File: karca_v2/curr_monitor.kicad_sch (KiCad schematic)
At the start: 25 parts, among them U30 INA180A4, U32 NUP4202

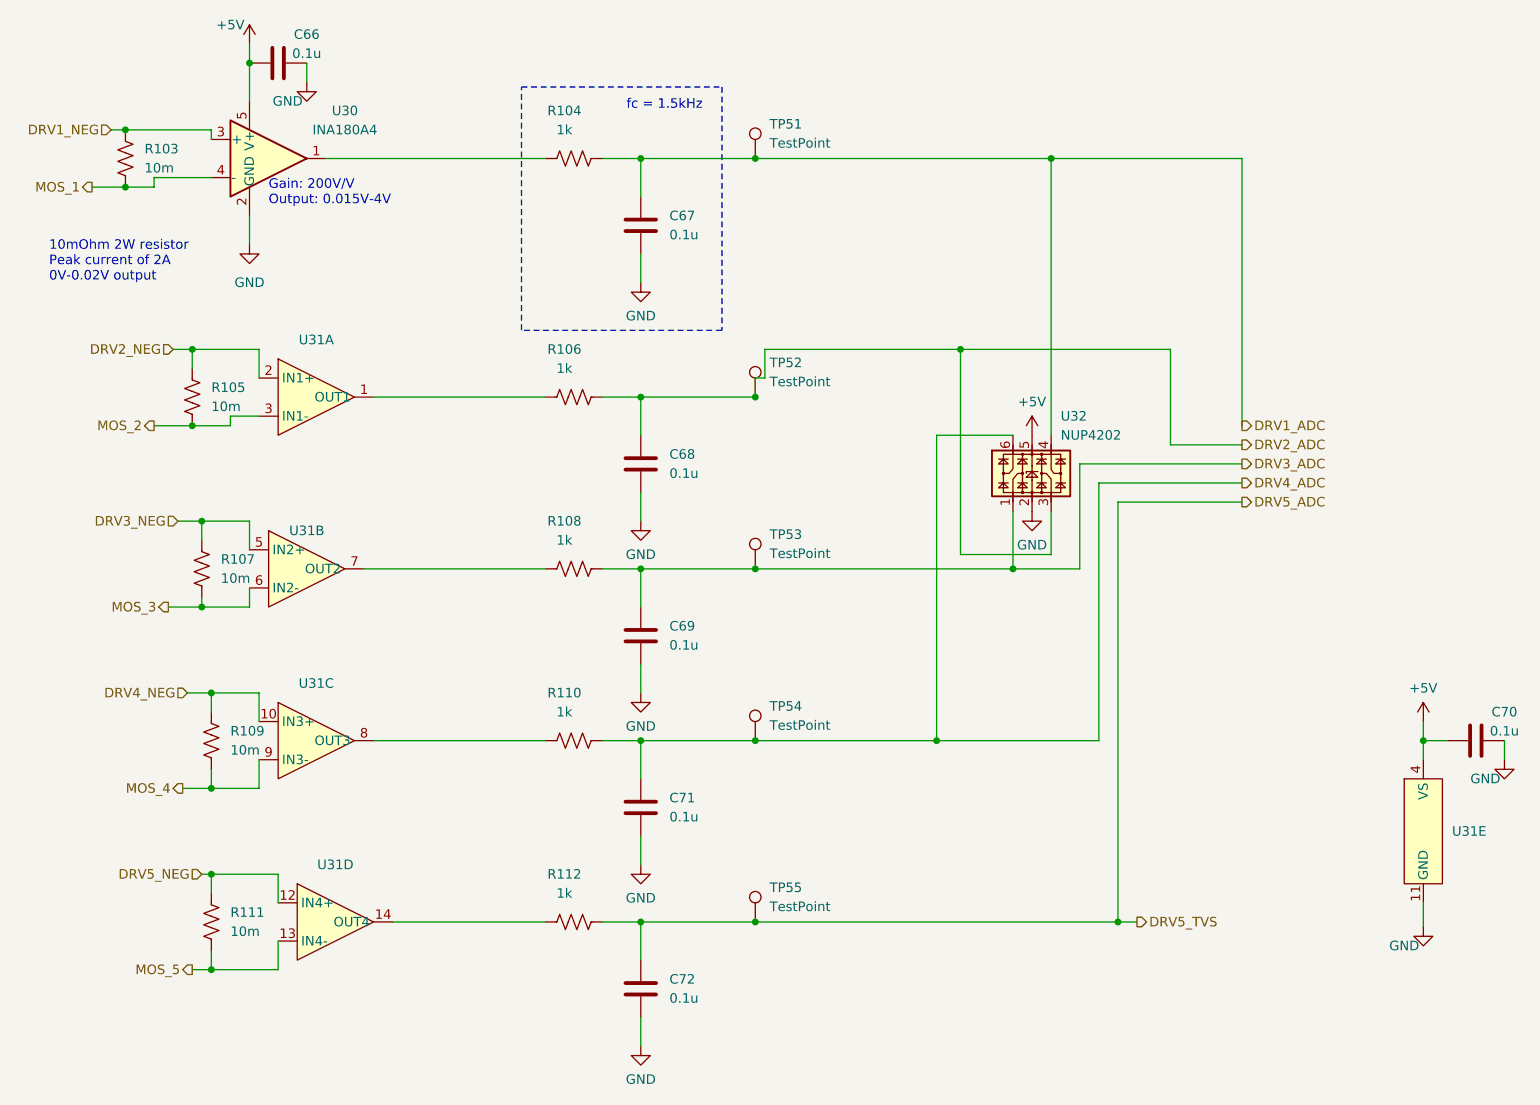
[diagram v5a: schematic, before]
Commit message: cleaned up documentation. Added production files and BOM. Marked Thermocouple components and THT components as DNP (excluded them from BOM too) to match version sent to JLCPCB for fabrication
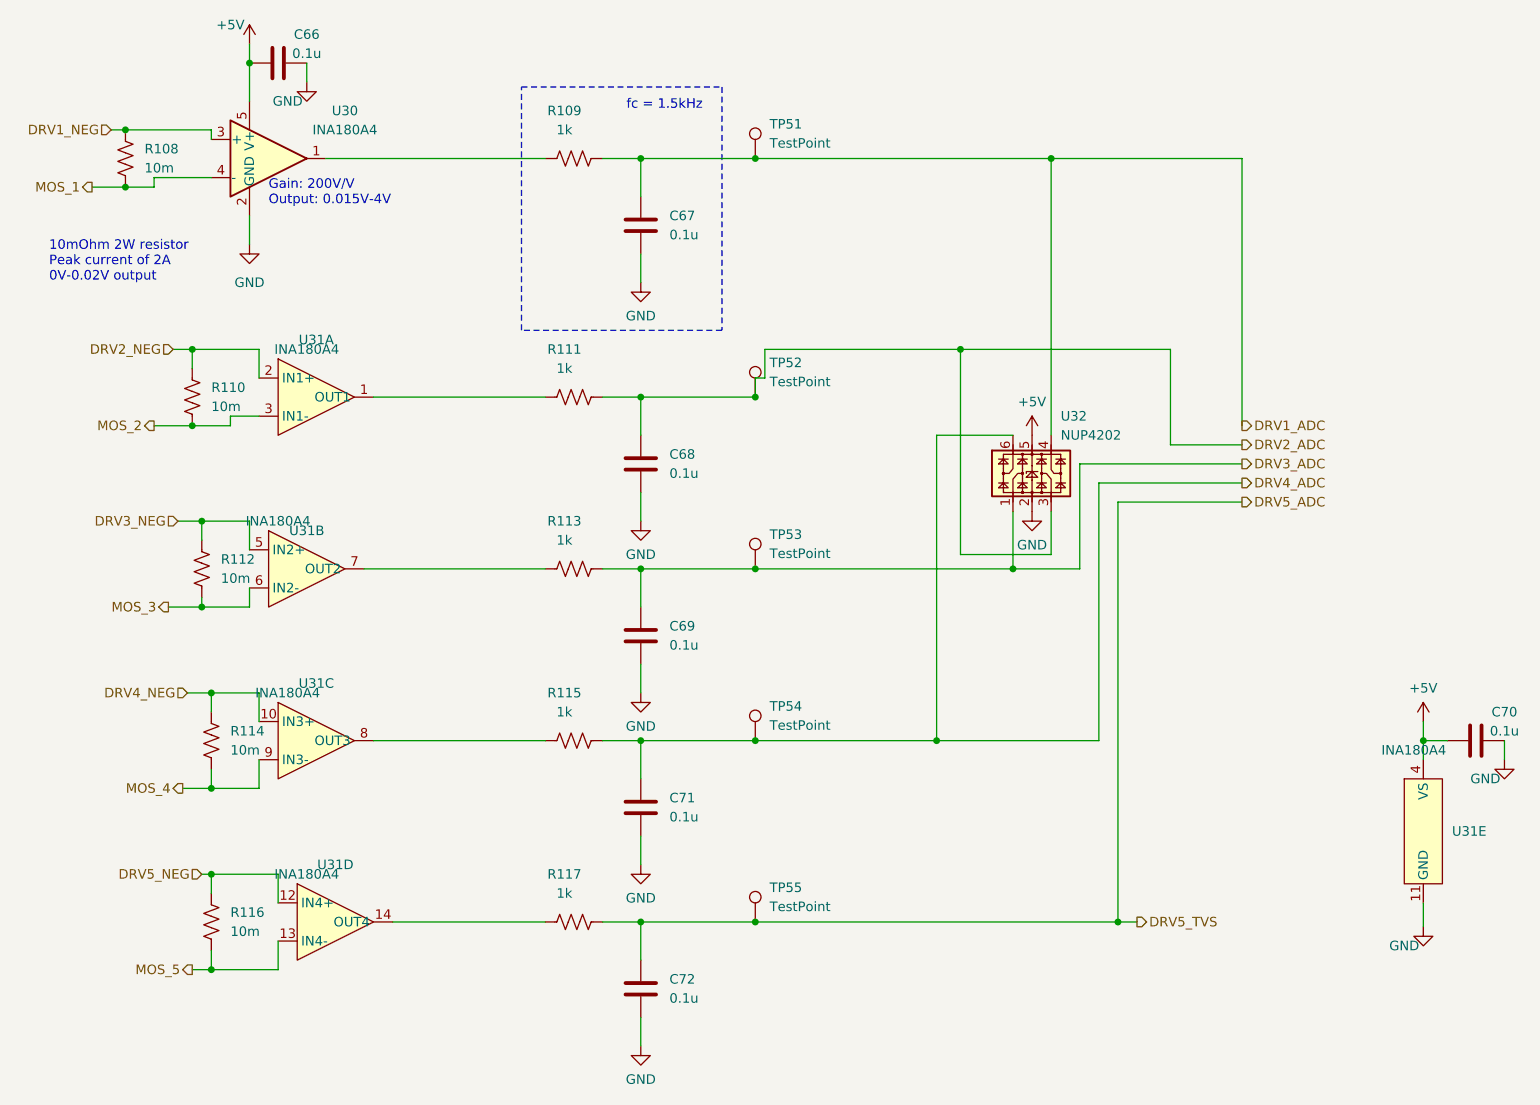
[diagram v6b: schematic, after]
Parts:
- R108: renamed from R103; footprint Resistor_SMD:R_1206_3216Metric -> Resistor_SMD:R_2512_6332Metric
- R110: renamed from R105; footprint Resistor_SMD:R_1206_3216Metric -> Resistor_SMD:R_2512_6332Metric
- R112: renamed from R107; footprint Resistor_SMD:R_1206_3216Metric -> Resistor_SMD:R_2512_6332Metric
- R114: renamed from R109; footprint Resistor_SMD:R_1206_3216Metric -> Resistor_SMD:R_2512_6332Metric
- R116: renamed from R111; footprint Resistor_SMD:R_1206_3216Metric -> Resistor_SMD:R_2512_6332Metric
- U31: value ~ -> INA180A4
- renumbered R104 to R109, R106 to R111, R108 to R113, R110 to R115, R112 to R117
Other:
- company: (none) -> Rice Eclipse
- title: (none) -> kARCA 2.0 Engine Control System
